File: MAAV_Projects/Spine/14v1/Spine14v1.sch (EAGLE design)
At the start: 84 parts, among them J7 MA04-1, Q1 MOSFET-NCHANNELBSS138, Q2 MOSFET-NCHANNELSMD, Q21 P-MOSFET-SO8POWER-PAK, Q22 P-MOSFET-SO8POWER-PAK, Q23 P-MOSFET-SO8POWER-PAK, Q24 P-MOSFET-SO8POWER-PAK, Q3 MOSFET-NCHANNELSMD, Q4 MOSFET-NCHANNELSMD, Q6 16MHz, Q7 CRYSTAL_16MHZ_SMD, U1 ATMEGA328-AU, U2 REG_3V_8SOIC

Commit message: started routing
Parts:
- removed C11: 4.7uF, rcl:C-USC0805
- removed LED2, LED3, LED4: GREEN, Jon_LIB:LEDCHIPLED_0603
- removed LED5: red, Jon_LIB:LEDCHIPLED_0603
- removed LED6: green, Jon_LIB:LEDCHIPLED_0603
- removed LED7: blue, Jon_LIB:LEDCHIPLED_0603
- removed R44, R47, R48: 750, Jon_LIB:R-USR0805
- removed S1: SWITCH-OFF-MOM_SMD_TACTILE, MAAV:SWITCH-OFF-MOM_SMD_TACTILE
- removed U2: REG_3V_8SOIC, MAAV:REG_3V_8SOIC
- added ATOM_POW, DJI_POW: POWER_CONN_VERT, MAAV:POWER_CONN_VERT
- added C15: 1.0uF, Jon_LIB:C-EUC0805
- added C16: 2.2uF, Jon_LIB:C-EUC0805
- added D1, D2: LED_RGB_CA, Jon_LIB:LED_RGB_CA
- added Q5: P-MOSFET-SO8POWER-PAK, Jon_LIB:P-MOSFET-SO8POWER-PAK
- added Q8: MOSFET-NCHANNELSMD, Jon_LIB:MOSFET-NCHANNELSMD
- added R10: 200, Jon_LIB:R-USR0603
- added R14: 100, Jon_LIB:R-USR0603
- added R7, R8: 2.2k, Jon_LIB:R-USR0603
- added S2: (no value), Jon_LIB:TACT_BUTTONSMD
- added U$1, U$6: CRYSTAL_403C11E16, imu:CRYSTAL_403C11E16
- added U3: XC6210, MAAV:XC6210
- C10: value 0.1uF -> 10nF; device rcl:C-USC0603 -> Jon_LIB:C-EUC0603
- C13, C14: device Jon_LIB:C-EUC0603 -> Jon_LIB:C-EUC0805
- C19, C20: value 22pF -> 10pF; DIGIKEY# 478-6200-1-ND -> 399-1049-1-ND
- C4: device rcl:C-USC0603 -> Jon_LIB:C-EUC0603
- LED1: device MAAV_13v1:JON_LIB_LEDCHIPLED_0603 -> Jon_LIB:LEDCHIPLED_0603
- MOUT0, MOUT1, MOUT2, MOUT3: value POWER_CONN -> POWER_CONN_VERT; device MAAV:POWER_CONN -> MAAV:POWER_CONN_VERT
- Q1: value MOSFET-NCHANNELBSS138 -> MOSFET-NCHANNELSMD; device SparkFun-DiscreteSemi:MOSFET-NCHANNELBSS138 -> Jon_LIB:MOSFET-NCHANNELSMD
- Q6: value 16MHz -> MOSFET-NCHANNELSMD; device crystal:CRYSTALHC49UP -> Jon_LIB:MOSFET-NCHANNELSMD
- Q7: value CRYSTAL_16MHZ_SMD -> MOSFET-NCHANNELSMD; device Jon_LIB:CRYSTAL_16MHZ_SMD -> Jon_LIB:MOSFET-NCHANNELSMD
- R1, R11, R12, R15, R2, R3, R9: device rcl:R-US_R0603 -> Jon_LIB:R-USR0603
- R13: value 250k -> 100; device rcl:R-US_R0603 -> Jon_LIB:R-USR0603
- R16: value 330 -> 100; device rcl:R-US_R0603 -> Jon_LIB:R-USR0603
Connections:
- removed net N$33: LED3.A, R47.1
- removed net N$34: LED4.A, R48.1
- removed net N$9: LED2.A, R44.1
- new net N$21: DJI_POW.P, Q5.D1
- new net N$22: Q6.D, R14.1
- new net N$23: D2.R, R10.2
- new net N$24: D2.G, R13.2
- new net N$25: D2.B, R14.2
- net +3V3: now also C16.1, U3.VOUT; no longer C11.1, R13.2, U2.OUT, U2.OUT2
- net +5V: now also ATOM_POW.P, C15.2, D1.A, D2.A, U3.CE, U3.VIN; no longer C10.1, LED5.A, LED6.A, LED7.A, U2.IN, U2.IN2
- net 5V_ENABLE: now also U$4.P$5; no longer U$4.P$2
- net A_XTAL1: now also U$6.2; no longer Q7.P$1
- net A_XTAL2: now also U$6.1; no longer Q7.P$2
- net GND: now also ATOM_POW.N, C15.1, C16.2, DJI_POW.N, MOUT0.N, MOUT1.N, MOUT2.N, MOUT3.N, Q6.S, Q7.S, Q8.S, R7.1, R8.1, S2.S, U$1.GND, U$4.P$6, U$6.GND, U3.GND; no longer C11.2, LED2.C, LED3.C, LED4.C, MOUT0.P2, MOUT1.P2, MOUT2.P2, MOUT3.P2, S1.P$2, U$4.P$1, U2./EN, U2.GND
- net KILL_5: now also U1.(ADC1)PC1
- net LED1: now also Q8.G; no longer R48.2
- net LED2: now also Q7.G; no longer R47.2
- net LED3: now also Q6.G; no longer R44.2
- net M_ENABLE: now also Q5.G, U$4.P$2; no longer U$4.P$5
- net M_EN_PRE: now also U$4.P$1; no longer U$4.P$6
- net N$10: now also R11.1, S2.P; no longer R13.1, U2.PG
- net N$12: now also Q8.D, R10.1; no longer R11.1, S1.P$1
- net N$15: now also MOUT1.P; no longer MOUT1.P1
- net N$16: now also MOUT2.P; no longer MOUT2.P1
- net N$17: now also MOUT3.P; no longer MOUT3.P1
- net N$19: now also D1.B; no longer LED7.C
- net N$2: now also MOUT0.P; no longer MOUT0.P1
- net N$20: now also Q7.D, R13.1; no longer C26.1, C3.1, C31.+, U$5.V_I
- net N$6: now also D1.R; no longer LED5.C
- net N$7: now also D1.G; no longer LED6.C
- net RESET: now also C10.1
- net SCL_3V3: now also R8.2
- net SDA_3V3: now also R7.2
- net T_OSC0: now also U$1.2; no longer Q6.2
- net T_OSC1: now also U$1.1; no longer Q6.1
- net V_BATT: now also C26.1, C3.1, C31.+, Q5.S1, U$5.V_I
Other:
- note added: "Check the sizes used in last years design"
- note added: "Power to Atom"
- note added: "Power to DJI"
- note added: "Still need... signal to DJI"
- note removed: "3V3 Power Supply"
- note removed: "Change to D# 535-9103-1-ND"
- note removed: "Consider an RGB LED like D# 754-1500-1-ND"
- note removed: "Kill Switch Signal Receiver"
- note removed: "Replace this componenet with something else"
- note removed: "Still need... Power to atom power to DJI"
- note removed: "Verify the orientation of this switch "up" should be "on""
- note removed: "these Holes look too small"
- moved on the sheet: C17, C18, LED1, R11, R16, R9

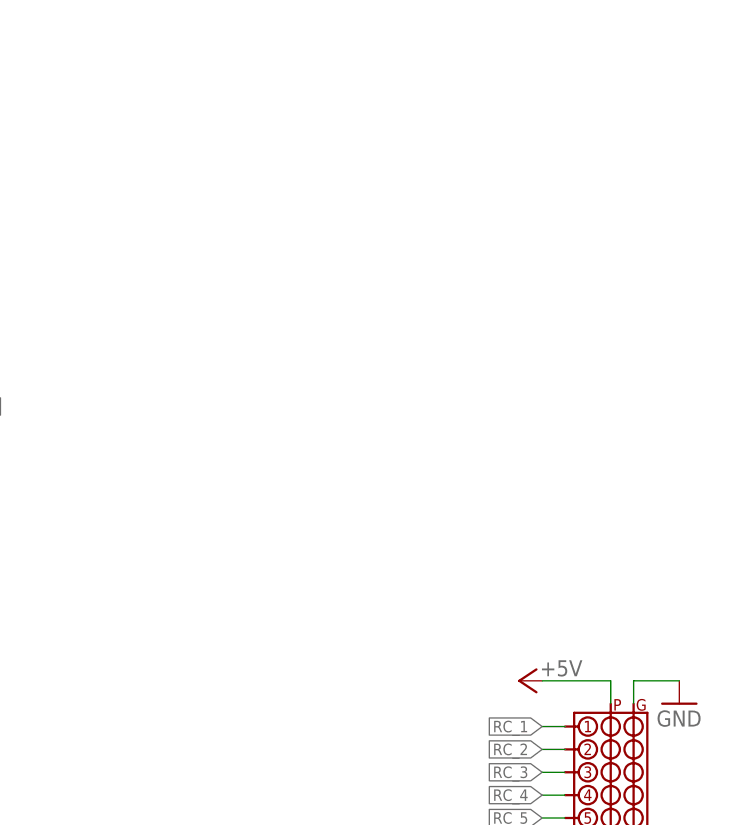
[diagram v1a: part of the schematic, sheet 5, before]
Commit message: routed some more (almost finished). Added some micro swtiches to Jon_LIB
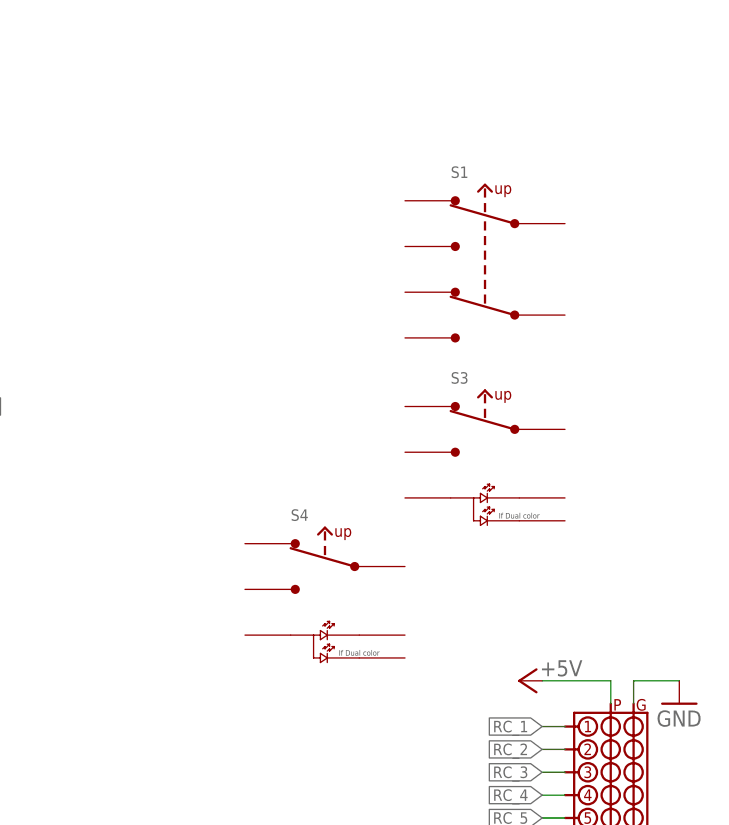
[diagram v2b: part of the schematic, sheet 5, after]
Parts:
- added S1: SWITCH_DPDT_VERT_TOGGLE, Jon_LIB:SWITCH_DPDT_VERT_TOGGLE
- added S3, S4: SWITCH_SPDT_ILUMINATED_2COLOR_VERT_ILLUMINATED, Jon_LIB:SWITCH_SPDT_ILUMINATED_2COLOR_VERT_ILLUMINATED
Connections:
- net KILL_4: now also U$3.PE2; no longer U$3.PE1
- net KILL_5: now also U$3.PE1; no longer U$3.PE2
- net KILL_6: now also U$3.PE0; no longer U$3.PE3
- net KILL_SIG: now also U$3.PE3; no longer U$3.PE0
- net LED1: now also U1.(ICP)PB0; no longer U1.(OC1)PB1
- net LED2: now also U1.(OC1)PB1; no longer U1.(ICP)PB0
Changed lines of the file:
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@@
 <part name="P+9" library="supply1" deviceset="+5V" device=""/>
 <part name="D2" library="Jon_LIB" deviceset="LED_RGB_CA" device=""/>
+<part name="S1" library="Jon_LIB" deviceset="SWITCH_DPDT" device="_VERT_TOGGLE"/>
+<part name="S3" library="Jon_LIB" deviceset="SWITCH_SPDT_ILUMINATED_2COLOR" device="_VERT_ILLUMINATED"/>
+<part name="S4" library="Jon_LIB" deviceset="SWITCH_SPDT_ILUMINATED_2COLOR" device="_VERT_ILLUMINATED"/>
 </parts>
 <sheets>
@@
 <net name="KILL_4" class="0">
 <segment>
+<wire x1="33.02" y1="73.66" x2="43.18" y2="73.66" width="0.1524" layer="91"/>
+<label x="33.02" y="73.66" size="1.27" layer="95" rot="MR0" xref="yes"/>
+<pinref part="U$3" gate="G$1" pin="PE2"/>
+</segment>
+</net>
+<net name="KILL_5" class="0">
+<segment>
+<wire x1="33.02" y1="71.12" x2="43.18" y2="71.12" width="0.1524" layer="91"/>
+<label x="33.02" y="71.12" size="1.27" layer="95" rot="MR0" xref="yes"/>
 <pinref part="U$3" gate="G$1" pin="PE1"/>
-<wire x1="38.1" y1="71.12" x2="43.18" y2="71.12" width="0.1524" layer="91"/>
-<label x="38.1" y="71.12" size="1.27" layer="95" rot="R180" xref="yes"/>
-</segment>
-</net>
-<net name="KILL_5" class="0">
-<segment>
-<pinref part="U$3" gate="G$1" pin="PE2"/>
-<wire x1="38.1" y1="73.66" x2="43.18" y2="73.66" width="0.1524" layer="91"/>
-<label x="38.1" y="73.66" size="1.27" layer="95" rot="R180" xref="yes"/>
 </segment>
 </net>
 <net name="KILL_6" class="0">
 <segment>
-<pinref part="U$3" gate="G$1" pin="PE3"/>
-<wire x1="38.1" y1="76.2" x2="43.18" y2="76.2" width="0.1524" layer="91"/>
-<label x="38.1" y="76.2" size="1.27" layer="95" rot="R180" xref="yes"/>
+<wire x1="33.02" y1="68.58" x2="43.18" y2="68.58" width="0.1524" layer="91"/>
+<label x="33.02" y="68.58" size="1.27" layer="95" rot="MR0" xref="yes"/>
+<pinref part="U$3" gate="G$1" pin="PE0"/>
 </segment>
 </net>
@@
 <net name="KILL_SIG" class="0">
 <segment>
-<pinref part="U$3" gate="G$1" pin="PE0"/>
-<wire x1="38.1" y1="68.58" x2="43.18" y2="68.58" width="0.1524" layer="91"/>
-<label x="38.1" y="68.58" size="1.27" layer="95" rot="R180" xref="yes"/>
+<wire x1="33.02" y1="76.2" x2="43.18" y2="76.2" width="0.1524" layer="91"/>
+<label x="33.02" y="76.2" size="1.27" layer="95" rot="MR0" xref="yes"/>
+<pinref part="U$3" gate="G$1" pin="PE3"/>
 </segment>
 </net>
@@
 <net name="LED1" class="0">
 <segment>
-<wire x1="170.18" y1="149.86" x2="175.26" y2="149.86" width="0.1524" layer="91"/>
-<pinref part="U1" gate="G$1" pin="(OC1)PB1"/>
-<label x="175.26" y="149.86" size="1.27" layer="95" xref="yes"/>
+<wire x1="170.18" y1="147.32" x2="175.26" y2="147.32" width="0.1524" layer="91"/>
+<label x="175.26" y="147.32" size="1.27" layer="95" rot="MR180" xref="yes"/>
+<pinref part="U1" gate="G$1" pin="(ICP)PB0"/>
 </segment>
 <segment>
@@
 <net name="LED2" class="0">
 <segment>
-<wire x1="175.26" y1="147.32" x2="170.18" y2="147.32" width="0.1524" layer="91"/>
-<pinref part="U1" gate="G$1" pin="(ICP)PB0"/>
-<label x="175.26" y="147.32" size="1.27" layer="95" xref="yes"/>
+<wire x1="175.26" y1="149.86" x2="170.18" y2="149.86" width="0.1524" layer="91"/>
+<label x="175.26" y="149.86" size="1.27" layer="95" rot="MR180" xref="yes"/>
+<pinref part="U1" gate="G$1" pin="(OC1)PB1"/>
 </segment>
 <segment>
@@
 <attribute name="VALUE" x="139.446" y="53.848" size="1.778" layer="96"/>
 </instance>
+<instance part="S1" gate="G$1" x="231.14" y="180.34"/>
+<instance part="S3" gate="G$1" x="231.14" y="157.48"/>
+<instance part="S4" gate="G$1" x="213.36" y="142.24"/>
 </instances>
 <busses>
